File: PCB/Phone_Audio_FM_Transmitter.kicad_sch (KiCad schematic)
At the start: 28 parts, among them J1 Vin, J2 Conn_Coaxial, J3 Conn_Coaxial, J4 USB_B_Micro, U2 Si4706, U3 Si4711, U4 ESP32-S3-WROOM-1

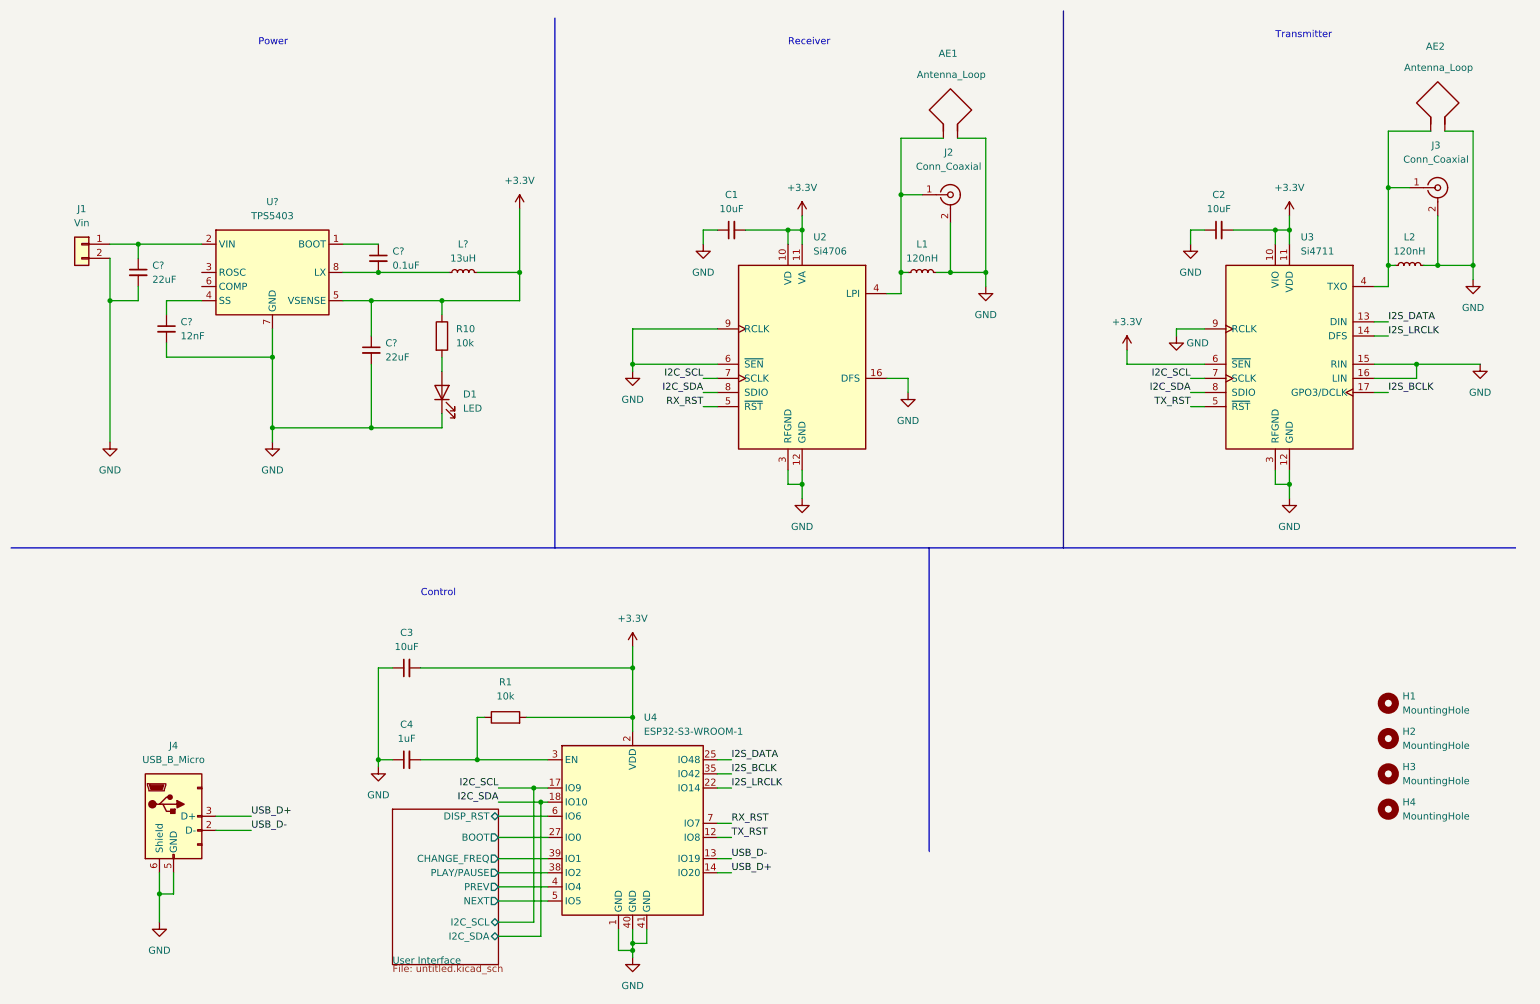
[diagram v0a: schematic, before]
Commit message: Added datasheets and PCB files
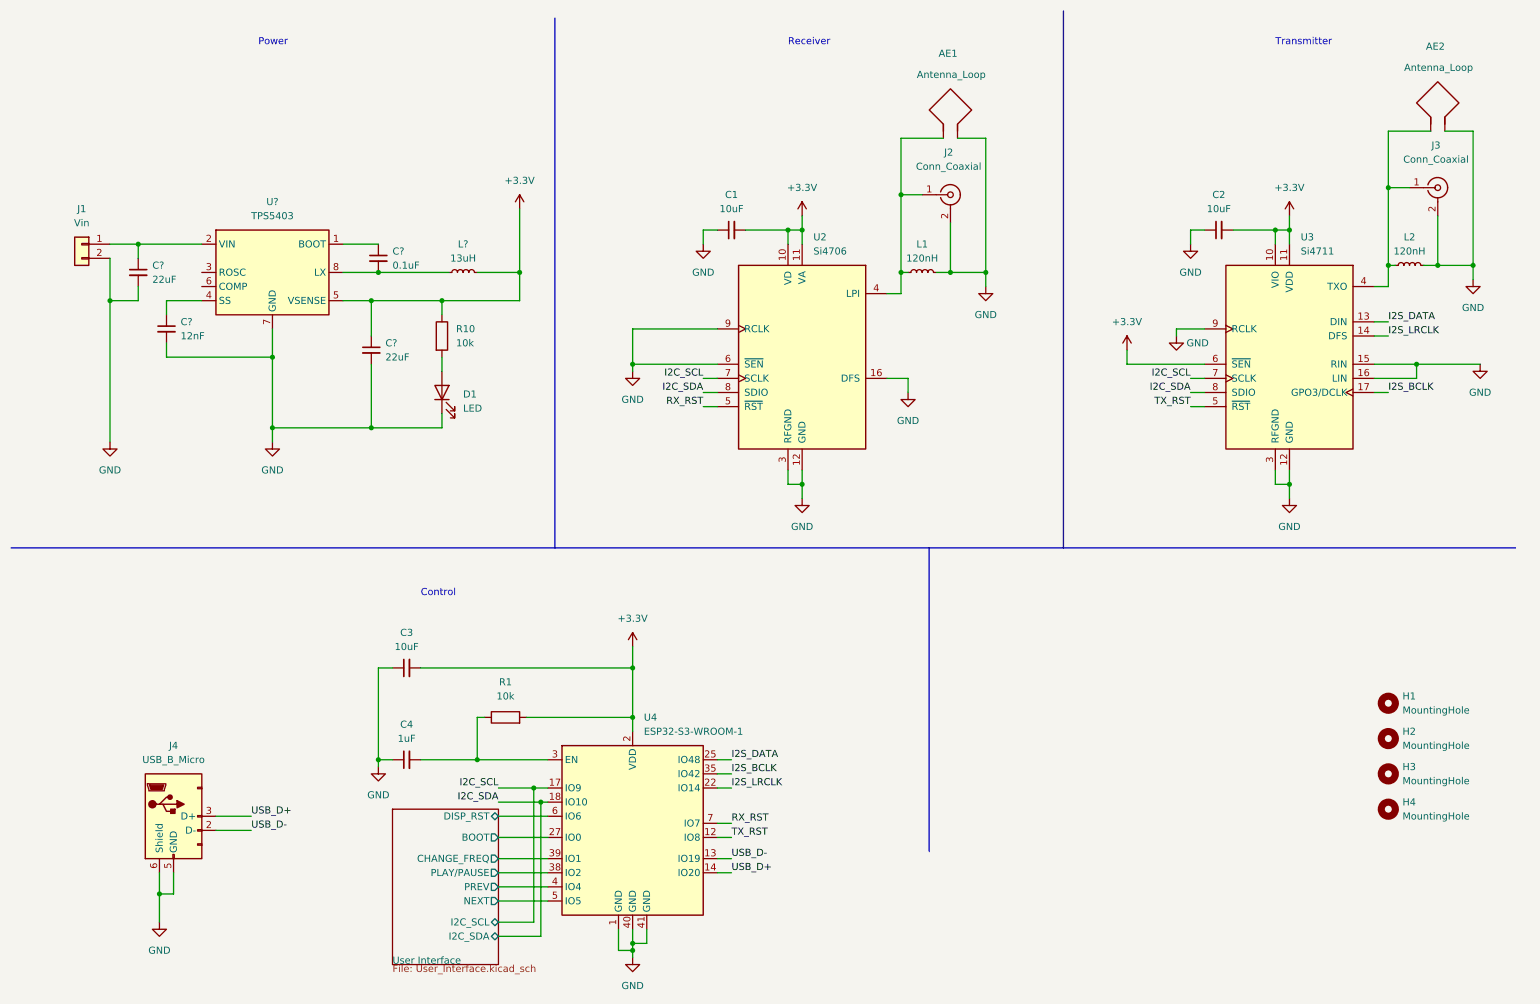
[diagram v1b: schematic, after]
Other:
- sheet User Interface: file untitled.kicad_sch -> User_Interface.kicad_sch

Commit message: Added voltage regulator components to finish schematic
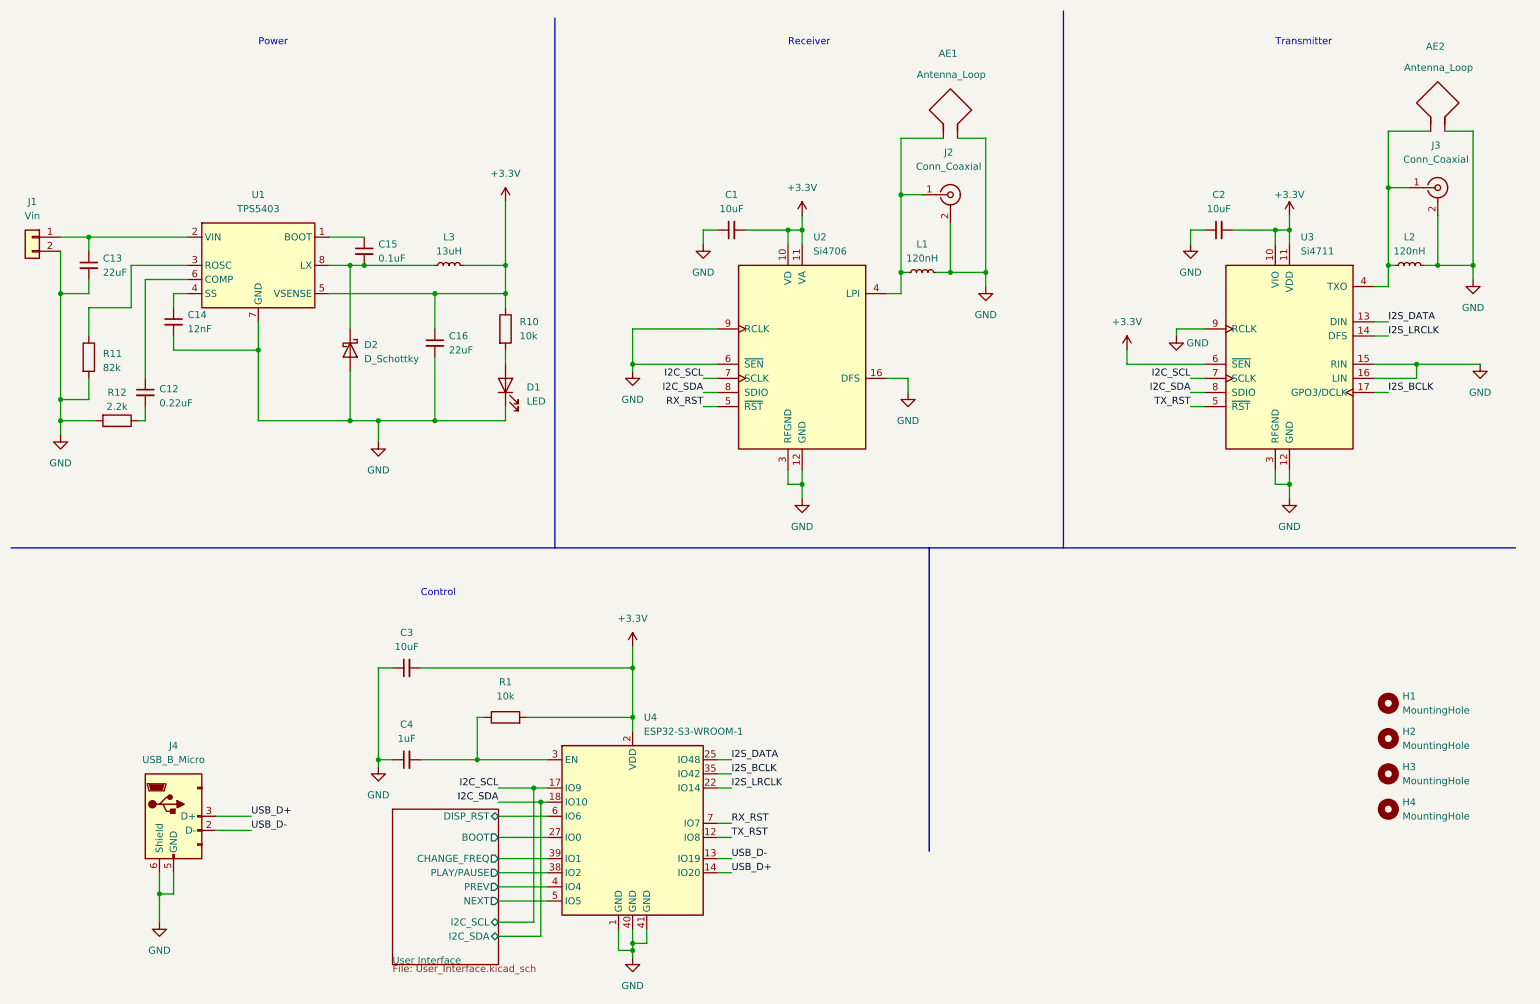
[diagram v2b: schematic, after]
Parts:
- added C12: 0.22uF, Capacitor_SMD:C_0805_2012Metric_Pad1.18x1.45mm_HandSolder, symbol Device:C_Small
- added D2: D_Schottky, Diode_SMD:D_0805_2012Metric_Pad1.15x1.40mm_HandSolder, symbol Device:D_Schottky
- added R11: 82k, Resistor_SMD:R_0805_2012Metric_Pad1.20x1.40mm_HandSolder, symbol Device:R
- added R12: 2.2k, Resistor_SMD:R_0805_2012Metric_Pad1.20x1.40mm_HandSolder, symbol Device:R
- C13, C14, C15, C16: renamed from C?; footprint (none) -> Capacitor_SMD:C_0805_2012Metric_Pad1.18x1.45mm_HandSolder
- L3: renamed from L?; footprint (none) -> Inductor_SMD:L_0805_2012Metric_Pad1.15x1.40mm_HandSolder
- gave numbers to parts that had none: 1
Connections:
- net GND: now also D2.2 (A), R11.2, R12.2
- net at U1.3 (ROSC): now also R11.1
- net at U1.6 (COMP): now also C12.1
- net at C15.2, L3.1, U1.8 (LX): now also D2.1 (K)
- new net: C12.2, R12.1
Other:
- moved on the sheet: C13, C14, C15, C16, D1, J1, L3, R10, U1

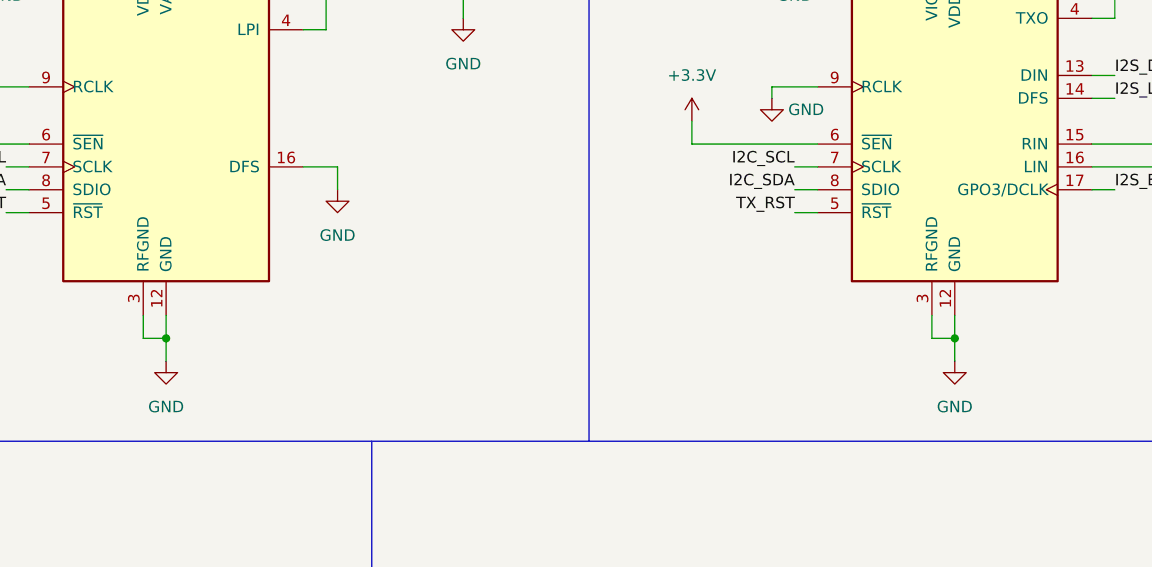
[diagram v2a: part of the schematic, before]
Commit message: Added first revision of layout. Needs antennae and possibly I2S test points.
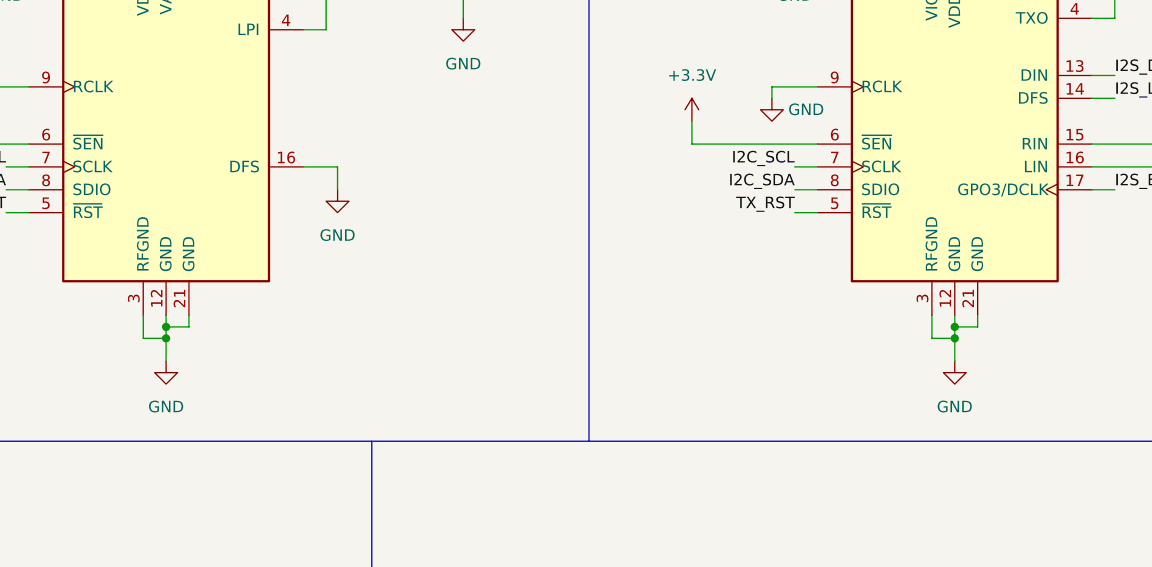
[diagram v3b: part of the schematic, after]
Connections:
- net GND: now also U2.21 (GND), U3.21 (GND)
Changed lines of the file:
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@@
   (junction (at 124.46 181.61) (diameter 0) (color 0 0 0 0)
   )
+  (junction (at 154.94 97.79) (diameter 0) (color 0 0 0 0)
+  )
   (junction (at 260.35 59.69) (diameter 0) (color 0 0 0 0)
   )
@@
   (junction (at 78.74 148.59) (diameter 0) (color 0 0 0 0)
   )
+  (junction (at 242.57 97.79) (diameter 0) (color 0 0 0 0)
+  )
   (junction (at 73.66 87.63) (diameter 0) (color 0 0 0 0)
   )
@@
     (stroke (width 0) (type default))
   )
+  (wire (pts (xy 245.11 97.79) (xy 242.57 97.79))
+    (stroke (width 0) (type default))
+  )
   (polyline (pts (xy 12.7 110.49) (xy 283.21 110.49))
     (stroke (width 0) (type default))
@@
     (stroke (width 0) (type default))
   )
+  (wire (pts (xy 157.48 96.52) (xy 157.48 97.79))
+    (stroke (width 0) (type default))
+  )
   (wire (pts (xy 180.34 36.83) (xy 172.72 36.83))
     (stroke (width 0) (type default))
@@
     (stroke (width 0) (type default))
   )
-  (wire (pts (xy 242.57 96.52) (xy 242.57 99.06))
+  (wire (pts (xy 242.57 96.52) (xy 242.57 97.79))
     (stroke (width 0) (type default))
   )
@@
     (stroke (width 0) (type default))
   )
+  (wire (pts (xy 154.94 97.79) (xy 154.94 99.06))
+    (stroke (width 0) (type default))
+  )
   (wire (pts (xy 139.7 148.59) (xy 142.24 148.59))
     (stroke (width 0) (type default))
@@
     (stroke (width 0) (type default))
   )
+  (wire (pts (xy 157.48 97.79) (xy 154.94 97.79))
+    (stroke (width 0) (type default))
+  )
   (wire (pts (xy 124.46 77.47) (xy 139.7 77.47))
     (stroke (width 0) (type default))
@@
     (stroke (width 0) (type default))
   )
-  (wire (pts (xy 154.94 96.52) (xy 154.94 99.06))
+  (wire (pts (xy 154.94 96.52) (xy 154.94 97.79))
     (stroke (width 0) (type default))
   )
@@
   )
   (wire (pts (xy 224.79 53.34) (xy 227.33 53.34))
+    (stroke (width 0) (type default))
+  )
+  (wire (pts (xy 242.57 97.79) (xy 242.57 99.06))
+    (stroke (width 0) (type default))
+  )
+  (wire (pts (xy 245.11 96.52) (xy 245.11 97.79))
     (stroke (width 0) (type default))
   )
@@
     (pin "11")
     (pin "12")
+    (pin "21")
     (pin "13")
     (pin "14")
@@
     (pin "11")
     (pin "12")
+    (pin "21")
     (pin "13")
     (pin "14")

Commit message: Finished Rev. 1 layout with Gerber files
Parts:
- removed AE1, AE2: Antenna_Loop, symbol Device:Antenna_Loop
- added J6: Rec, Connector_Molex:Molex_KK-254_AE-6410-02A_1x02_P2.54mm_Vertical, symbol Connector_Generic:Conn_01x02
- added J7: Trans, Connector_Molex:Molex_KK-254_AE-6410-02A_1x02_P2.54mm_Vertical, symbol Connector_Generic:Conn_01x02
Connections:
- net GND: now also J6.2 (Pin_2), J7.2 (Pin_2)
- net at J2.1 (In), L1.2, U2.4 (LPI): now also J6.1 (Pin_1)
- net at J3.1 (In), L2.2, U3.4 (TXO): now also J7.1 (Pin_1)
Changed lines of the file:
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@@
+    )
+  )
+  (symbol (lib_name "Conn_01x02_2") (lib_id "Connector_Generic:Conn_01x02") (at 267.97 30.48 90) (unit 1)
+    (in_bom yes) (on_board yes) (dnp no)
+    (property "Reference" "J7" (at 267.335 33.02 90)
+      (effects (font (size 1.27 1.27)) (justify left))
+    )
+    (property "Value" "Trans" (at 269.875 33.02 90)
+      (effects (font (size 1.27 1.27)) (justify left))
+    )
+    (property "Footprint" "Connector_Molex:Molex_KK-254_AE-6410-02A_1x02_P2.54mm_Vertical" (at 266.7 30.48 0)
+      (effects (font (size 1.27 1.27)) hide)
+    )
+    (property "Datasheet" "~" (at 267.97 30.48 0)
+      (effects (font (size 1.27 1.27)) hide)
+    )
+    (pin "1")
+    (pin "2")
+    (instances
+      (project "Phone_Audio_FM_Transmitter"
+        (path "/7013f989-dc97-4bbb-aad5-389a17fd7be1"
+          (reference "J7") (unit 1)
+        )
+      )
     )
   )
@@
     (pin "11")
     (pin "12")
-    (pin "21")
     (pin "13")
     (pin "14")
@@
     (pin "2")
     (pin "20")
+    (pin "21")
     (pin "3")
     (pin "4")
@@
     (pin "11")
     (pin "12")
-    (pin "21")
     (pin "13")
     (pin "14")
@@
     (pin "2")
     (pin "20")
+    (pin "21")
     (pin "3")
     (pin "4")
@@
     )
   )
-  (symbol (lib_id "Device:Antenna_Loop") (at 270.51 30.48 0) (mirror y) (unit 1)
+  (symbol (lib_id "power:+3.3V") (at 101.6 48.26 0) (unit 1)
+    (in_bom yes) (on_board yes) (dnp no) (fields_autoplaced)
+    (property "Reference" "#PWR0104" (at 101.6 52.07 0)
+      (effects (font (size 1.27 1.27)) hide)
+    )
+    (property "Value" "+3.3V" (at 101.6 43.18 0)
+      (effects (font (size 1.27 1.27)))
+    )
+    (property "Footprint" "" (at 101.6 48.26 0)
+      (effects (font (size 1.27 1.27)) hide)
+    )
+    (property "Datasheet" "" (at 101.6 48.26 0)
+      (effects (font (size 1.27 1.27)) hide)
+    )
+    (pin "1")
+    (instances
+      (project "Phone_Audio_FM_Transmitter"
+        (path "/7013f989-dc97-4bbb-aad5-389a17fd7be1"
+          (reference "#PWR0104") (unit 1)
+        )
+      )
+    )
+  )
+  (symbol (lib_name "Conn_01x02_1") (lib_id "Connector_Generic:Conn_01x02") (at 180.34 31.75 90) (unit 1)
     (in_bom yes) (on_board yes) (dnp no)
-    (property "Reference" "AE2" (at 270.51 20.32 0)
-      (effects (font (size 1.27 1.27)) (justify left))
-    )
-    (property "Value" "Antenna_Loop" (at 275.59 24.13 0)
-      (effects (font (size 1.27 1.27)) (justify left))
-    )
-    (property "Footprint" "" (at 270.51 30.48 0)
-      (effects (font (size 1.27 1.27)) hide)
-    )
-    (property "Datasheet" "~" (at 270.51 30.48 0)
-      (effects (font (size 1.27 1.27)) hide)
-    )
-    (pin "1")
-    (pin "2")
-    (instances
-      (project "Phone_Audio_FM_Transmitter"
-        (path "/7013f989-dc97-4bbb-aad5-389a17fd7be1"
-          (reference "AE2") (unit 1)
-        )
-      )
-    )
-  )
-  (symbol (lib_id "power:+3.3V") (at 101.6 48.26 0) (unit 1)
-    (in_bom yes) (on_board yes) (dnp no) (fields_autoplaced)
-    (property "Reference" "#PWR0104" (at 101.6 52.07 0)
-      (effects (font (size 1.27 1.27)) hide)
-    )
-    (property "Value" "+3.3V" (at 101.6 43.18 0)
-      (effects (font (size 1.27 1.27)))
-    )
-    (property "Footprint" "" (at 101.6 48.26 0)
-      (effects (font (size 1.27 1.27)) hide)
-    )
-    (property "Datasheet" "" (at 101.6 48.26 0)
-      (effects (font (size 1.27 1.27)) hide)
-    )
-    (pin "1")
-    (instances
-      (project "Phone_Audio_FM_Transmitter"
-        (path "/7013f989-dc97-4bbb-aad5-389a17fd7be1"
-          (reference "#PWR0104") (unit 1)
+    (property "Reference" "J6" (at 179.705 34.29 90)
+      (effects (font (size 1.27 1.27)) (justify left))
+    )
+    (property "Value" "Rec" (at 182.245 34.29 90)
+      (effects (font (size 1.27 1.27)) (justify left))
+    )
+    (property "Footprint" "Connector_Molex:Molex_KK-254_AE-6410-02A_1x02_P2.54mm_Vertical" (at 177.8 31.75 0)
+      (effects (font (size 1.27 1.27)) hide)
+    )
+    (property "Datasheet" "~" (at 180.34 31.75 0)
+      (effects (font (size 1.27 1.27)) hide)
+    )
+    (pin "1")
+    (pin "2")
+    (instances
+      (project "Phone_Audio_FM_Transmitter"
+        (path "/7013f989-dc97-4bbb-aad5-389a17fd7be1"
+          (reference "J6") (unit 1)
         )
       )
@@
         )
       )
-    )
-  )
-  (symbol (lib_id "Device:Antenna_Loop") (at 182.88 31.75 0) (mirror y) (unit 1)
-    (in_bom yes) (on_board yes) (dnp no)
-    (property "Reference" "AE1" (at 182.88 21.59 0)
-      (effects (font (size 1.27 1.27)) (justify left))
-    )
-    (property "Value" "Antenna_Loop" (at 187.96 25.4 0)
-      (effects (font (size 1.27 1.27)) (justify left))
-    )
-    (property "Footprint" "" (at 182.88 31.75 0)
-      (effects (font (size 1.27 1.27)) hide)
-    )
-    (property "Datasheet" "~" (at 182.88 31.75 0)
-      (effects (font (size 1.27 1.27)) hide)
-    )
-    (pin "1")
-    (pin "2")
-    (instances
-      (project "Phone_Audio_FM_Transmitter"
-        (path "/7013f989-dc97-4bbb-aad5-389a17fd7be1"
-          (reference "AE1") (unit 1)
-        )
-      )
